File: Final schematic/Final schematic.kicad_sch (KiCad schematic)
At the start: 39 parts, among them J1 PJ-102AH, J2 Conn_01x06, J3 Conn_02x03_Odd_Even, SW1 Omron_B3F_SPST, SW2 Omron_B3F_SPST, SW3 Omron_B3F_SPST, SW4 Omron_B3F_SPST, U1 ATmega328-PU, U2 L7805, U3 MAX7219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

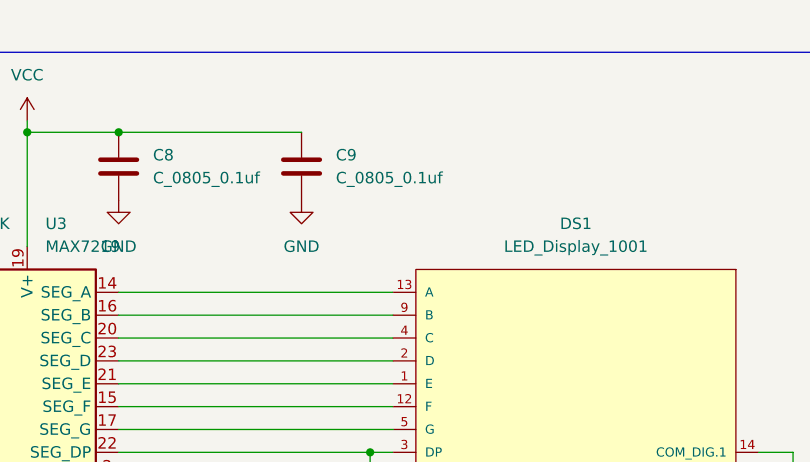
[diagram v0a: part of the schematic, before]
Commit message: schematic update
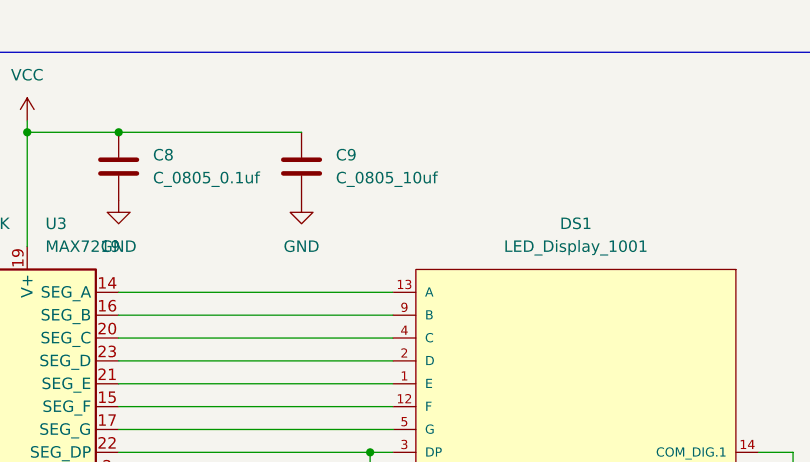
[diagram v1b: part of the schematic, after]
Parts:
- removed C9: C_0805_0.1uf, footprints:C_0805_2012Metric, symbol HPS:C_0805_0.1uf
- added C9: C_0805_10uf, footprints:C_0805_2012Metric, symbol HPS:C_0805_10uf
- U2: footprint (none) -> footprints:TO-252-2; Digikey PN (none) -> 497-7255-1-ND; MFG (none) -> STMicroelectronics; MPN (none) -> L7805CDT-TR
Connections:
- net GND: now also C9.2
- net VCC: now also C9.1
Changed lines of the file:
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@@
     (property "Reference" "U2" (id 0) (at 64.77 124.46 0))
     (property "Value" "L7805" (id 1) (at 64.77 127 0))
-    (property "Footprint" "" (id 2) (at 65.405 135.89 0)
+    (property "Footprint" "footprints:TO-252-2" (id 2) (at 65.405 135.89 0)
       (effects (font (size 1.27 1.27) italic) (justify left) hide)
     )
     (property "Datasheet" "http://www.st.com/content/ccc/resource/technical/document/datasheet/41/4f/b3/b0/12/d4/47/88/CD00000444.pdf/files/CD00000444.pdf/jcr:content/translations/en.CD00000444.pdf" (id 3) (at 64.77 133.35 0)
+      (effects (font (size 1.27 1.27)) hide)
+    )
+    (property "Digikey PN" "497-7255-1-ND" (id 4) (at 64.77 132.08 0)
+      (effects (font (size 1.27 1.27)) hide)
+    )
+    (property "MPN" "L7805CDT-TR" (id 5) (at 64.77 132.08 0)
+      (effects (font (size 1.27 1.27)) hide)
+    )
+    (property "MFG" "STMicroelectronics" (id 6) (at 64.77 132.08 0)
       (effects (font (size 1.27 1.27)) hide)
     )
@@
     )
     (pin "1")
-  )
-  (symbol (lib_id "HPS:C_0805_0.1uf") (at 171.45 27.94 0) (unit 1)
-    (in_bom yes) (on_board yes) (fields_autoplaced)
-    (property "Reference" "C9" (id 0) (at 175.26 26.6699 0)
-      (effects (font (size 1.27 1.27)) (justify left))
-    )
-    (property "Value" "C_0805_0.1uf" (id 1) (at 175.26 29.2099 0)
-      (effects (font (size 1.27 1.27)) (justify left))
-    )
-    (property "Footprint" "footprints:C_0805_2012Metric" (id 2) (at 172.4152 31.75 0)
-      (effects (font (size 1.27 1.27)) hide)
-    )
-    (property "Datasheet" "https://datasheets.avx.com/X7RDielectric.pdf" (id 3) (at 172.085 25.4 0)
-      (effects (font (size 1.27 1.27)) hide)
-    )
-    (property "MFG" "AVX Corporation" (id 4) (at 171.45 34.29 0)
-      (effects (font (size 1.27 1.27)) hide)
-    )
-    (property "MPN" "08055C104KAT2A" (id 5) (at 171.45 36.83 0)
-      (effects (font (size 1.27 1.27)) hide)
-    )
-    (property "Digikey PN" "478-1395-1-ND" (id 6) (at 171.45 41.91 0)
-      (effects (font (size 1.27 1.27)) hide)
-    )
-    (property "Mouser PN" "N/A" (id 7) (at 171.45 44.45 0)
-      (effects (font (size 1.27 1.27)) hide)
-    )
-    (property "Voltage" "N/A" (id 8) (at 171.45 46.99 0)
-      (effects (font (size 1.27 1.27)) hide)
-    )
-    (property "Dielectric" "N/A" (id 9) (at 171.45 46.99 0)
-      (effects (font (size 1.27 1.27)) hide)
-    )
-    (property "Tolerance" "N/A" (id 10) (at 171.45 46.99 0)
-      (effects (font (size 1.27 1.27)) hide)
-    )
-    (pin "1")
-    (pin "2")
   )
   (symbol (lib_id "HPS:GND") (at 171.45 31.75 0) (unit 1)
@@
     (pin "2")
   )
+  (symbol (lib_id "HPS:C_0805_10uf") (at 171.45 27.94 0) (unit 1)
+    (in_bom yes) (on_board yes) (fields_autoplaced)
+    (property "Reference" "C9" (id 0) (at 175.26 26.6699 0)
+      (effects (font (size 1.27 1.27)) (justify left))
+    )
+    (property "Value" "C_0805_10uf" (id 1) (at 175.26 29.2099 0)
+      (effects (font (size 1.27 1.27)) (justify left))
+    )
+    (property "Footprint" "footprints:C_0805_2012Metric" (id 2) (at 172.4152 31.75 0)
+      (effects (font (size 1.27 1.27)) hide)
+    )
+    (property "Datasheet" "https://search.murata.co.jp/Ceramy/image/img/A01X/G101/ENG/GRM21BR61E106KA73-01.pdf" (id 3) (at 172.085 25.4 0)
+      (effects (font (size 1.27 1.27)) hide)
+    )
+    (property "MFG" "Murata Electronics" (id 4) (at 171.45 34.29 0)
+      (effects (font (size 1.27 1.27)) hide)
+    )
+    (property "MPN" "GRM21BR61E106KA73L" (id 5) (at 171.45 36.83 0)
+      (effects (font (size 1.27 1.27)) hide)
+    )
+    (property "Digikey PN" "490-5523-1-ND" (id 6) (at 171.45 41.91 0)
+      (effects (font (size 1.27 1.27)) hide)
+    )
+    (property "Mouser PN" "N/A" (id 7) (at 171.45 44.45 0)
+      (effects (font (size 1.27 1.27)) hide)
+    )
+    (property "Voltage" "N/A" (id 8) (at 171.45 46.99 0)
+      (effects (font (size 1.27 1.27)) hide)
+    )
+    (property "Dielectric" "N/A" (id 9) (at 171.45 46.99 0)
+      (effects (font (size 1.27 1.27)) hide)
+    )
+    (property "Tolerance" "N/A" (id 10) (at 171.45 46.99 0)
+      (effects (font (size 1.27 1.27)) hide)
+    )
+    (pin "1")
+    (pin "2")
+  )
   (symbol (lib_id "HPS:C_0805_0.1uf") (at 53.34 135.89 0) (unit 1)
     (in_bom yes) (on_board yes)
@@
       (reference "C8") (unit 1) (value "C_0805_0.1uf") (footprint "footprints:C_0805_2012Metric")
     )
-    (path "/51129121-8d68-4c6f-9308-dd863814bc8e"
-      (reference "C9") (unit 1) (value "C_0805_0.1uf") (footprint "footprints:C_0805_2012Metric")
+    (path "/eccfb4b4-d4b1-4624-8685-61493e1f560f"
+      (reference "C9") (unit 1) (value "C_0805_10uf") (footprint "footprints:C_0805_2012Metric")
     )
     (path "/a825c272-5958-4faf-bb1b-76ac2c2ea861"
@@
     )
     (path "/3175aaf7-ed7c-443e-92bd-e02fdce19c0b"
-      (reference "U2") (unit 1) (value "L7805") (footprint "")
+      (reference "U2") (unit 1) (value "L7805") (footprint "footprints:TO-252-2")
     )
     (path "/04611237-e0c9-49a7-812a-ad2cbff5a815"

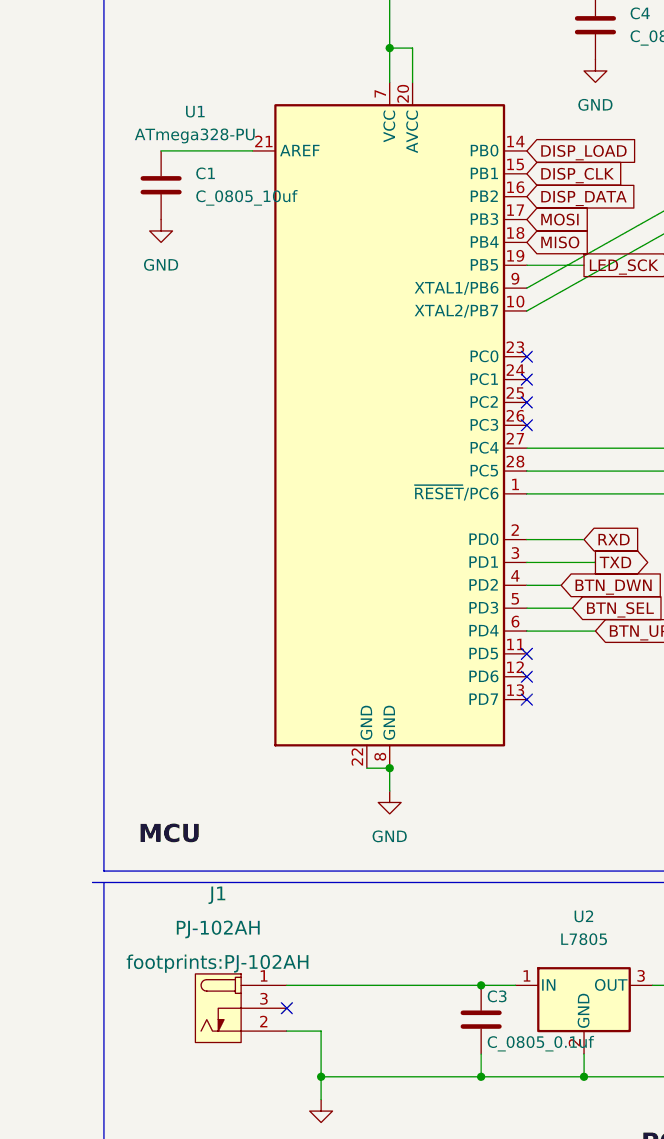
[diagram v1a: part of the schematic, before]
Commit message: A few updates before manufacturing
Hi Ganiru, just fixing a few small things on the board and schematic before we send it for manufacturing.
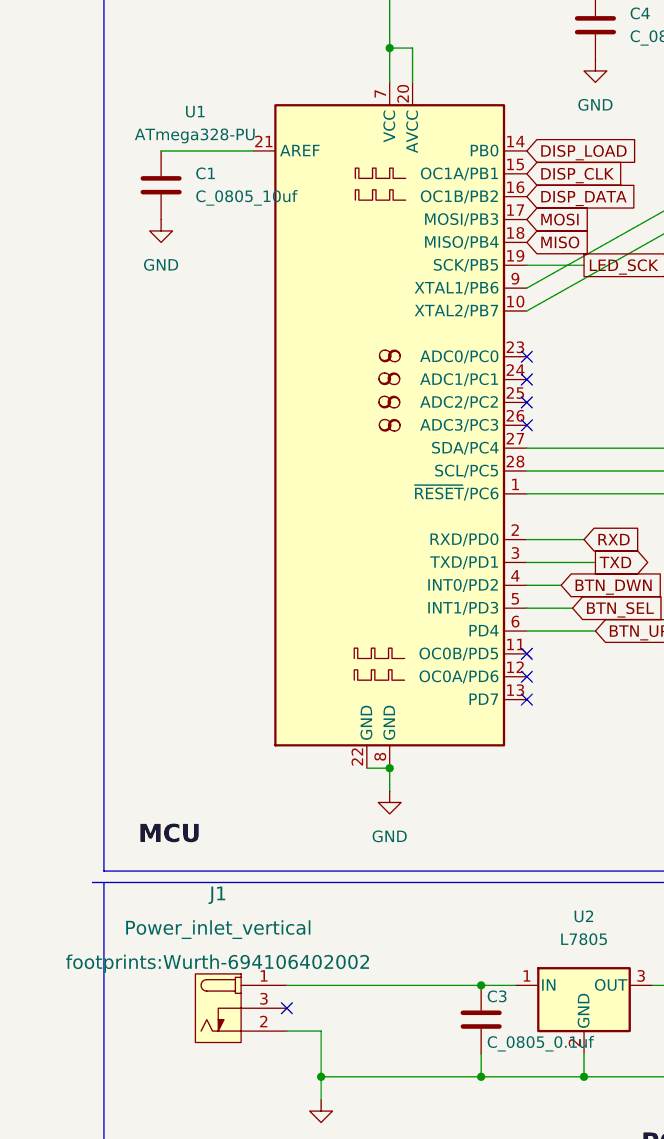
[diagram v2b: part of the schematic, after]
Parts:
- removed J1: PJ-102AH, footprints:PJ-102AH, symbol HPS:PJ-102AH
- added J1: Power_inlet_vertical, footprints:Wurth-694106402002, symbol HPS:Power_inlet_vertical
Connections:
- net GND: now also J1.2 (OUT)
- net at C3.1, U2.1 (IN): now also J1.1 (POLE)
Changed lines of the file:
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@@
     )
-  )
-  (symbol (lib_id "HPS:PJ-102AH") (at 26.67 134.62 0) (unit 1)
-    (in_bom yes) (on_board yes) (fields_autoplaced)
-    (property "Reference" "J1" (id 0) (at 24.13 121.92 0)
-      (effects (font (size 1.524 1.524)))
-    )
-    (property "Value" "PJ-102AH" (id 1) (at 24.13 125.73 0)
-      (effects (font (size 1.524 1.524)))
-    )
-    (property "Footprint" "footprints:PJ-102AH" (id 2) (at 24.13 129.54 0)
-      (effects (font (size 1.524 1.524)))
-    )
-    (property "Datasheet" "https://www.cuidevices.com/product/resource/pj-102ah.pdf" (id 3) (at 28.194 146.558 0)
-      (effects (font (size 1.524 1.524)) hide)
-    )
-    (property "MFG" "CUI Devices" (id 4) (at 26.67 152.4 0)
-      (effects (font (size 1.27 1.27)) hide)
-    )
-    (property "MPN" "PJ-102AH" (id 5) (at 26.67 154.94 0)
-      (effects (font (size 1.27 1.27)) hide)
-    )
-    (property "Digikey PN" "CP-102AH-ND" (id 6) (at 28.194 160.147 0)
-      (effects (font (size 1.27 1.27)) hide)
-    )
-    (property "Mouser PN" "490-PJ-102AH" (id 7) (at 26.67 157.353 0)
-      (effects (font (size 1.27 1.27)) hide)
-    )
-    (pin "1")
-    (pin "2")
-    (pin "3")
   )
   (symbol (lib_id "HPS:MAX7219") (at 140.97 62.23 0) (unit 1)
@@
     (pin "2")
   )
-  (symbol (lib_id "HPS:MountingHole") (at 157.48 152.4 0) (unit 1)
+  (symbol (lib_name "MountingHole_1") (lib_id "HPS:MountingHole") (at 157.48 152.4 0) (unit 1)
     (in_bom yes) (on_board yes) (fields_autoplaced)
     (property "Reference" "H3" (id 0) (at 160.02 151.1299 0)
@@
     (pin "1")
   )
-  (symbol (lib_id "HPS:MountingHole") (at 137.16 152.4 0) (unit 1)
+  (symbol (lib_name "MountingHole_3") (lib_id "HPS:MountingHole") (at 137.16 152.4 0) (unit 1)
     (in_bom yes) (on_board yes) (fields_autoplaced)
     (property "Reference" "H1" (id 0) (at 139.7 151.1299 0)
@@
     (pin "1")
     (pin "2")
+  )
+  (symbol (lib_id "HPS:Power_inlet_vertical") (at 26.67 134.62 0) (unit 1)
+    (in_bom yes) (on_board yes) (fields_autoplaced)
+    (property "Reference" "J1" (id 0) (at 24.13 121.92 0)
+      (effects (font (size 1.524 1.524)))
+    )
+    (property "Value" "Power_inlet_vertical" (id 1) (at 24.13 125.73 0)
+      (effects (font (size 1.524 1.524)))
+    )
+    (property "Footprint" "footprints:Wurth-694106402002" (id 2) (at 24.13 129.54 0)
+      (effects (font (size 1.524 1.524)))
+    )
+    (property "Datasheet" "https://www.we-online.com/katalog/datasheet/6941xx402002.pdf" (id 3) (at 28.194 146.558 0)
+      (effects (font (size 1.524 1.524)) hide)
+    )
+    (property "MFG" "Wurth" (id 4) (at 26.67 152.4 0)
+      (effects (font (size 1.27 1.27)) hide)
+    )
+    (property "MPN" "694106402002" (id 5) (at 26.67 154.94 0)
+      (effects (font (size 1.27 1.27)) hide)
+    )
+    (property "Digikey PN" "732-5931-ND" (id 6) (at 28.194 160.147 0)
+      (effects (font (size 1.27 1.27)) hide)
+    )
+    (pin "1")
+    (pin "2")
+    (pin "3")
   )
   (symbol (lib_id "HPS:R_0805_4.7K") (at 91.44 64.77 0) (unit 1)
@@
     (pin "2")
   )
-  (symbol (lib_id "HPS:MountingHole") (at 157.48 160.02 0) (unit 1)
+  (symbol (lib_name "MountingHole_2") (lib_id "HPS:MountingHole") (at 157.48 160.02 0) (unit 1)
     (in_bom yes) (on_board yes) (fields_autoplaced)
     (property "Reference" "H4" (id 0) (at 160.02 158.7499 0)
@@
       (reference "H4") (unit 1) (value "MountingHole") (footprint "footprints:MountingHole_3.2mm_M3")
     )
-    (path "/037a8e6d-4abc-4b60-8de6-cb87d7aa4e51"
-      (reference "J1") (unit 1) (value "PJ-102AH") (footprint "footprints:PJ-102AH")
+    (path "/8b3358ef-0f4a-4c12-b83c-d24ba81ea238"
+      (reference "J1") (unit 1) (value "Power_inlet_vertical") (footprint "footprints:Wurth-694106402002")
     )
     (path "/4c37e47c-98bc-4a5e-8ce0-7f67b646829b"
